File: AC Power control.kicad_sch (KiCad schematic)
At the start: 18 parts, among them IC3 ULN2803CDWR, J6 USB_B_Micro, J7 Conn_02x05_Top_Bottom, U3 USBLC6-2SC6

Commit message: update
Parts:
- D8: footprint (none) -> LED_SMD:LED_0805_2012Metric
- renumbered IC3 to U8
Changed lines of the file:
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@@
 			)
 		)
-		(property "Footprint" ""
+		(property "Footprint" "LED_SMD:LED_0805_2012Metric"
 			(at 217.17 80.01 0)
 			(effects
@@
 		(dnp no)
 		(fields_autoplaced yes)
-		(property "Reference" "IC3"
+		(property "Reference" "U8"
 			(at 134.62 49.53 0)
 			(effects
@@
 			(project ""
 				(path "/c703575f-b97a-4282-ae81-d5777b8a5a01/2e427d26-78ca-4cc9-965e-91a8c72f7160"
-					(reference "IC3")
+					(reference "U8")
 					(unit 1)
 				)

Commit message: Done ERC + Documentation
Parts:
- R63: renamed from R47; value 0R -> 22R
- R64: renamed from R48; value 0R -> 22R
- U7: renamed from U8; MPN (none) -> ULN2803CDWR; Manufacturer_Part_Number ULN2803CDWR -> (none)
- renumbered D8 to D12, D7 to D13, J6 to J10, J7 to J9, R35 to R54, R36 to R55, R37 to R56, R38 to R57, R39 to R58, R40 to R59, R42 to R60, R41 to R61, R49 to R62, R43 to R65, U3 to U8
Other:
- note added: "EXT_5V Input or Output"

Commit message: Initial Review Changes
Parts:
- added F3: Polyfuse, Fuse:Fuse_1206_3216Metric, symbol Device:Polyfuse
- added TP10: 5V, TestPoint:TestPoint_Keystone_5000-5004_Miniature, symbol Connector:TestPoint
- added TP8: D+, TestPoint:TestPoint_Pad_D1.0mm, symbol Connector:TestPoint
- added TP9: D-, TestPoint:TestPoint_Pad_D1.0mm, symbol Connector:TestPoint
- J10: value USB_B_Micro -> USB FS
- J9: value Conn_02x05_Top_Bottom -> Relay IO
- renumbered R54 to R55, R55 to R56, R56 to R57, R57 to R58, R58 to R59, R59 to R60, R60 to R61, R61 to R62, R62 to R63, R63 to R64, R64 to R65, R65 to R66
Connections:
- net +5V: now also TP10.1
- net USB_OTG_FS_DN: now also TP9.1
- net USB_OTG_FS_DP: now also TP8.1
- net USB_OTG_FS_VBUS: now also F3.1; no longer J10.1 (VBUS)
- new net: F3.2, J10.1 (VBUS)
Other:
- company: (none) -> _electronic_projects
- title: (none) -> DeskNode-F4
- moved on the sheet: D12, D13, J10, R63, R64, R65, R66, U8

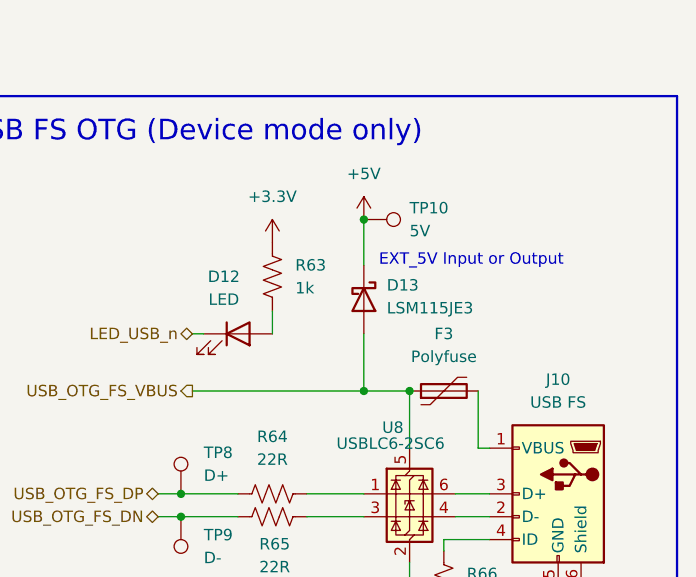
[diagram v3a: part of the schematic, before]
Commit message: MPNs updated
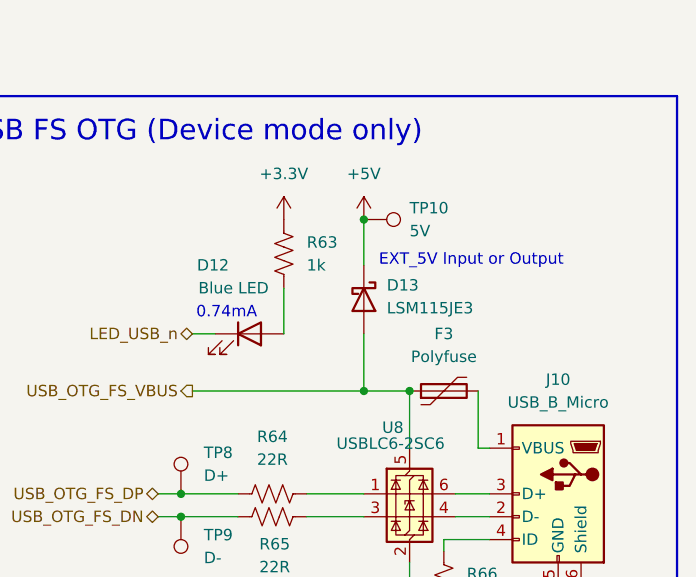
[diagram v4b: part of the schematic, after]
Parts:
- D12: value LED -> Blue LED; MPN (none) -> APT2012LVBC/D
- J10: value USB FS -> USB_B_Micro; footprint Connector_USB:USB_Micro-B_GCT_USB3076-30-A -> footprints:USB_Micro-B_GCT_USB3076-30-A
- R55, R56, R57, R58, R59, R60, R61, R62: MPN (none) -> RC0603FR-0710KL
- R63: MPN (none) -> RC0603FR-071KL
- R64, R65: MPN (none) -> RC0603FR-0722RL
- R66: MPN (none) -> RC0603FR-07100KL
- TP10: MPN (none) -> 5001
- U8: MPN (none) -> USBLC6-2SC6
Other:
- note added: "0.74mA"
- moved on the sheet: R63

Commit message: Layout placement
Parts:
- removed J9: Relay IO, Connector_PinHeader_2.54mm:PinHeader_2x05_P2.54mm_Vertical, symbol Connector_Generic:Conn_02x05_Top_Bottom
- added J9: Relay IO, Connector_PinHeader_2.54mm:PinHeader_2x05_P2.54mm_Vertical, symbol Connector_Generic:Conn_02x05_Odd_Even
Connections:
- net +12V: now also J9.1 (Pin_1)
- net CH1: now also J9.3 (Pin_3)
- net CH2: now also J9.5 (Pin_5)
- net CH3: now also J9.7 (Pin_7)
- net CH4: now also J9.9 (Pin_9)
- net CH5: now also J9.4 (Pin_4)
- net CH6: now also J9.6 (Pin_6)
- net CH7: now also J9.8 (Pin_8)
- net CH8: now also J9.10 (Pin_10)
- net GND: now also J9.2 (Pin_2)
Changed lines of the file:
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@@
 	(wire
 		(pts
-			(xy 101.6 144.78) (xy 99.06 144.78)
-		)
-		(stroke
-			(width 0)
-			(type default)
-		)
-	)
-	(wire
-		(pts
 			(xy 153.67 67.31) (xy 148.59 67.31)
 		)
@@
 	(wire
 		(pts
-			(xy 99.06 137.16) (xy 110.49 137.16)
-		)
-		(stroke
-			(width 0)
-			(type default)
-		)
-	)
-	(wire
-		(pts
 			(xy 243.84 113.03) (xy 243.84 114.3)
 		)
@@
 	(wire
 		(pts
-			(xy 83.82 147.32) (xy 86.36 147.32)
-		)
-		(stroke
-			(width 0)
-			(type default)
-		)
-	)
-	(wire
-		(pts
 			(xy 153.67 72.39) (xy 148.59 72.39)
 		)
@@
 	(wire
 		(pts
-			(xy 83.82 139.7) (xy 86.36 139.7)
+			(xy 83.82 142.24) (xy 86.36 142.24)
 		)
 		(stroke
@@
 	(wire
 		(pts
-			(xy 101.6 147.32) (xy 99.06 147.32)
+			(xy 248.92 102.87) (xy 243.84 102.87)
 		)
 		(stroke
@@
 	(wire
 		(pts
-			(xy 83.82 142.24) (xy 86.36 142.24)
+			(xy 54.61 74.93) (xy 54.61 90.17)
 		)
 		(stroke
@@
 	(wire
 		(pts
-			(xy 248.92 102.87) (xy 243.84 102.87)
+			(xy 220.98 97.79) (xy 214.63 97.79)
 		)
 		(stroke
@@
 	(wire
 		(pts
-			(xy 54.61 74.93) (xy 54.61 90.17)
+			(xy 107.95 97.79) (xy 107.95 102.87)
 		)
 		(stroke
@@
 	(wire
 		(pts
-			(xy 220.98 97.79) (xy 214.63 97.79)
+			(xy 247.65 86.36) (xy 247.65 92.71)
 		)
 		(stroke
@@
 	(wire
 		(pts
-			(xy 107.95 97.79) (xy 107.95 102.87)
+			(xy 101.6 144.78) (xy 99.06 144.78)
 		)
 		(stroke
@@
 	(wire
 		(pts
-			(xy 83.82 144.78) (xy 86.36 144.78)
+			(xy 234.95 80.01) (xy 234.95 86.36)
 		)
 		(stroke
@@
 	(wire
 		(pts
-			(xy 247.65 86.36) (xy 247.65 92.71)
+			(xy 83.82 144.78) (xy 86.36 144.78)
 		)
 		(stroke
@@
 	(wire
 		(pts
-			(xy 234.95 80.01) (xy 234.95 86.36)
+			(xy 48.26 59.69) (xy 100.33 59.69)
 		)
 		(stroke
@@
 	(wire
 		(pts
-			(xy 48.26 59.69) (xy 100.33 59.69)
+			(xy 101.6 147.32) (xy 99.06 147.32)
 		)
 		(stroke
@@
 	(wire
 		(pts
-			(xy 101.6 142.24) (xy 99.06 142.24)
+			(xy 99.06 137.16) (xy 110.49 137.16)
 		)
 		(stroke
@@
 	(wire
 		(pts
+			(xy 101.6 139.7) (xy 99.06 139.7)
+		)
+		(stroke
+			(width 0)
+			(type default)
+		)
+	)
+	(wire
+		(pts
 			(xy 153.67 64.77) (xy 148.59 64.77)
 		)
@@
 	(wire
 		(pts
-			(xy 76.2 137.16) (xy 86.36 137.16)
+			(xy 115.57 77.47) (xy 115.57 81.28)
 		)
 		(stroke
@@
 	(wire
 		(pts
-			(xy 115.57 77.47) (xy 115.57 81.28)
+			(xy 77.47 102.87) (xy 85.09 102.87)
 		)
 		(stroke
@@
 	(wire
 		(pts
-			(xy 77.47 102.87) (xy 85.09 102.87)
+			(xy 69.85 97.79) (xy 69.85 102.87)
 		)
 		(stroke
@@
 	(wire
 		(pts
-			(xy 69.85 97.79) (xy 69.85 102.87)
+			(xy 153.67 74.93) (xy 148.59 74.93)
 		)
 		(stroke
@@
 	(wire
 		(pts
-			(xy 153.67 74.93) (xy 148.59 74.93)
+			(xy 76.2 137.16) (xy 86.36 137.16)
+		)
+		(stroke
+			(width 0)
+			(type default)
+		)
+	)
+	(wire
+		(pts
+			(xy 83.82 147.32) (xy 86.36 147.32)
 		)
 		(stroke
@@
 	(wire
 		(pts
-			(xy 101.6 139.7) (xy 99.06 139.7)
+			(xy 101.6 142.24) (xy 99.06 142.24)
 		)
 		(stroke
@@
 	(wire
 		(pts
+			(xy 83.82 139.7) (xy 86.36 139.7)
+		)
+		(stroke
+			(width 0)
+			(type default)
+		)
+	)
+	(wire
+		(pts
 			(xy 215.9 86.36) (xy 234.95 86.36)
 		)
@@
 		(on_board yes)
 		(dnp no)
-		(fields_autoplaced yes)
 		(property "Reference" "F3"
-			(at 243.84 80.01 90)
+			(at 243.84 79.248 90)
 			(effects
 				(font
@@
 		)
 		(property "Value" "Polyfuse"
-			(at 243.84 82.55 90)
+			(at 243.84 81.788 90)
 			(effects
 				(font
@@
 		)
 		(property "MPN" "NANOSMDC075F-2"
-			(at 243.84 86.36 90)
+			(at 243.84 84.328 90)
 			(effects
 				(font
-					(size 1.27 1.27)
+					(size 0.889 0.889)
 				)
-				(hide yes)
 			)
 		)
@@
 		)
 		(property "MPN" "APT2012LVBC/D"
-			(at 222.25 80.01 0)
+			(at 221.996 83.82 0)
 			(effects
 				(font
 					(size 1.27 1.27)
 				)
-				(hide yes)
 			)
 		)
@@
 		(dnp no)
 		(property "Reference" "J10"
-			(at 256.54 85.09 0)
+			(at 256.54 83.312 0)
 			(effects
 				(font
@@
 		)
 		(property "Value" "USB_B_Micro"
-			(at 256.54 87.63 0)
+			(at 256.54 85.852 0)
 			(effects
 				(font
@@
 		)
 		(property "MPN" "USB3076-30-A"
-			(at 256.54 97.79 0)
+			(at 256.54 88.646 0)
 			(effects
 				(font
 					(size 1.27 1.27)
 				)
-				(hide yes)
 			)
 		)
@@
 	)
 	(symbol
-		(lib_id "Connector_Generic:Conn_02x05_Top_Bottom")
-		(at 91.44 142.24 0)
+		(lib_id "Device:R_US")
+		(at 224.79 97.79 270)
 		(unit 1)
 		(exclude_from_sim no)
@@
 		(dnp no)
 		(fields_autoplaced yes)
-		(property "Reference" "J9"
-			(at 92.71 130.81 0)
+		(property "Reference" "R64"
+			(at 224.79 91.44 90)
 			(effects
 				(font
@@
 			)
 		)
-		(property "Value" "Relay IO"
-			(at 92.71 133.35 0)
+		(property "Value" "22R"
+			(at 224.79 93.98 90)
 			(effects
 				(font
@@
 			)
 		)
-		(property "Footprint" "Connector_PinHeader_2.54mm:PinHeader_2x05_P2.54mm_Vertical"
-			(at 91.44 142.24 0)
+		(property "Footprint" "Resistor_SMD:R_0603_1608Metric"
+			(at 224.536 98.806 90)
 			(effects
 				(font
@@
 		)
 		(property "Datasheet" "~"
-			(at 91.44 142.24 0)
+			(at 224.79 97.79 0)
 			(effects
 				(font
@@
 			)
 		)
-		(property "Description" "Generic connector, double row, 02x05, top/bottom pin numbering scheme (row 1: 1...pins_per_row, row2: pins_per_row+1 ... num_pins), script generated (kicad-library-utils/schlib/autogen/connector/)"
-			(at 91.44 142.24 0)
+		(property "Description" "RES 22 OHM 1% 1/10W 0603"
+			(at 224.79 97.79 0)
 			(effects
 				(font
@@
 		)
 		(property "Manufacturer_Part_Number" ""
-			(at 91.44 142.24 0)
+			(at 224.79 97.79 90)
 			(effects
 				(font
@@
 			)
 		)
-		(pin "9"
-		)
-		(pin "10"
-		)
-		(pin "3"
-		)
-		(pin "4"
+		(property "MPN" "RC0603FR-0722RL"
+			(at 224.79 97.79 90)
+			(effects
+				(font
+					(size 1.27 1.27)
+				)
+				(hide yes)
+			)
 		)
-		(pin "5"
+		(pin "2"
 		)
 		(pin "1"
 		)
-		(pin "7"
-		)
-		(pin "8"
-		)
-		(pin "6"
-		)
-		(pin "2"
-		)
 		(instances
-			(project ""
+			(project "STM32 Microcontroller Board"
 				(path "/c703575f-b97a-4282-ae81-d5777b8a5a01/2e427d26-78ca-4cc9-965e-91a8c72f7160"
-					(reference "J9")
+					(reference "R64")
 					(unit 1)
 				)
@@
 	)
 	(symbol
-		(lib_id "Device:R_US")
-		(at 224.79 97.79 270)
+		(lib_id "Connector_Generic:Conn_02x05_Odd_Even")
+		(at 91.44 142.24 0)
 		(unit 1)
 		(exclude_from_sim no)
@@
 		(dnp no)
 		(fields_autoplaced yes)
-		(property "Reference" "R64"
-			(at 224.79 91.44 90)
+		(property "Reference" "J9"
+			(at 92.71 130.81 0)
 			(effects
 				(font
@@
 			)
 		)
-		(property "Value" "22R"
-			(at 224.79 93.98 90)
+		(property "Value" "Relay IO"
+			(at 92.71 133.35 0)
 			(effects
 				(font
@@
 			)
 		)
-		(property "Footprint" "Resistor_SMD:R_0603_1608Metric"
-			(at 224.536 98.806 90)
+		(property "Footprint" "Connector_PinHeader_2.54mm:PinHeader_2x05_P2.54mm_Vertical"
+			(at 91.44 142.24 0)
 			(effects
 				(font
@@
 		)
 		(property "Datasheet" "~"
-			(at 224.79 97.79 0)
+			(at 91.44 142.24 0)
 			(effects
 				(font
@@
 			)
 		)
-		(property "Description" "RES 22 OHM 1% 1/10W 0603"
-			(at 224.79 97.79 0)
+		(property "Description" "Generic connector, double row, 02x05, odd/even pin numbering scheme (row 1 odd numbers, row 2 even numbers), script generated (kicad-library-utils/schlib/autogen/connector/)"
+			(at 91.44 142.24 0)
 			(effects
 				(font
@@
 			)
 		)
-		(property "Manufacturer_Part_Number" ""
-			(at 224.79 97.79 90)
-			(effects
-				(font
-					(size 1.27 1.27)
-				)
-				(hide yes)
-			)
+		(pin "4"
 		)
-		(property "MPN" "RC0603FR-0722RL"
-			(at 224.79 97.79 90)
-			(effects
-				(font
-					(size 1.27 1.27)
-				)
-				(hide yes)
-			)
+		(pin "3"
 		)
-		(pin "2"
+		(pin "5"
+		)
+		(pin "7"
+		)
+		(pin "10"
 		)
 		(pin "1"
 		)
+		(pin "9"
+		)
+		(pin "6"
+		)
+		(pin "2"
+		)
+		(pin "8"
+		)
 		(instances
-			(project "STM32 Microcontroller Board"
+			(project ""
 				(path "/c703575f-b97a-4282-ae81-d5777b8a5a01/2e427d26-78ca-4cc9-965e-91a8c72f7160"
-					(reference "R64")
+					(reference "J9")
 					(unit 1)
 				)

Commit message: Layout Routing
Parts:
- removed TP8: D+, TestPoint:TestPoint_Pad_D1.0mm, symbol Connector:TestPoint
- removed TP9: D-, TestPoint:TestPoint_Pad_D1.0mm, symbol Connector:TestPoint
- added H1, H2, H3, H4: MountingHole, MountingHole:MountingHole_3.2mm_M3_Pad, symbol Mechanical:MountingHole
- F3: MPN NANOSMDC075F-2 -> NANOSMDC075
- J10: MPN USB3076-30-A -> USB3076-30
- U8: value USBLC6-2SC6 -> USBLC6-2
- renumbered D12 to D13, D13 to D14, R55 to R57, R56 to R58, R57 to R59, R58 to R60, R59 to R61, R60 to R62, R61 to R63, R62 to R64, R64 to R65, R65 to R66, R63 to R67, R66 to R68, TP10 to TP8
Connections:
- net USB_OTG_FS_VBUS: no longer U8.5 (VBUS)
- net at F3.2, J10.1 (VBUS): now also U8.5 (VBUS)
- net USB_FS_DN: now reaches R66.2, U8.3 (I/O2)
- net USB_FS_DP: now reaches R65.1, U8.1 (I/O1)
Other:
- moved on the sheet: D13, D14, F3, R65, R66, R67, TP8

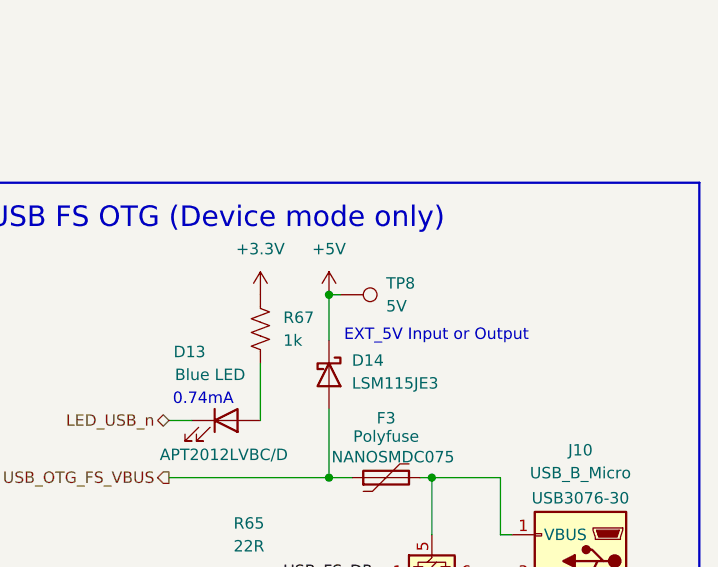
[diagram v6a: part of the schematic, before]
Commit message: Layout - 12V Power path
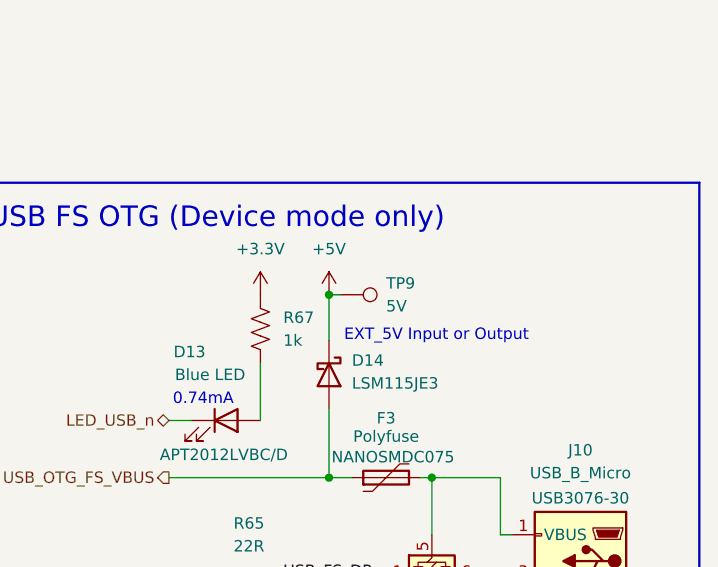
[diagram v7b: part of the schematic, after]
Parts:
- renumbered TP8 to TP9
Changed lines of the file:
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@@
 		(dnp no)
 		(fields_autoplaced yes)
-		(property "Reference" "TP8"
+		(property "Reference" "TP9"
 			(at 234.95 64.7699 90)
 			(effects
@@
 			(project "STM32 Microcontroller Board"
 				(path "/c703575f-b97a-4282-ae81-d5777b8a5a01/2e427d26-78ca-4cc9-965e-91a8c72f7160"
-					(reference "TP8")
+					(reference "TP9")
 					(unit 1)
 				)

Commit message: Review files
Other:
- company: _electronic_projects -> (none)
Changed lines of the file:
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@@
 		(title "DeskNode-F4")
 		(rev "A")
-		(company "_electronic_projects")
-		(comment 1 "Wajahatulla Sharif")
-		(comment 2 "Designed by ")
 	)
 	(rectangle
